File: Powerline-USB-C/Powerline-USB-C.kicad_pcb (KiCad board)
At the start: 2 copper layers, 14 x 100 mm, 17 parts, among them J1 USB-C 6pin, J2 Eurorack 10pin Power Connector, J3 Eurorack 10pin Power Connector, U1 CH224K, U2 N7812-1C, U3 N7812-1C

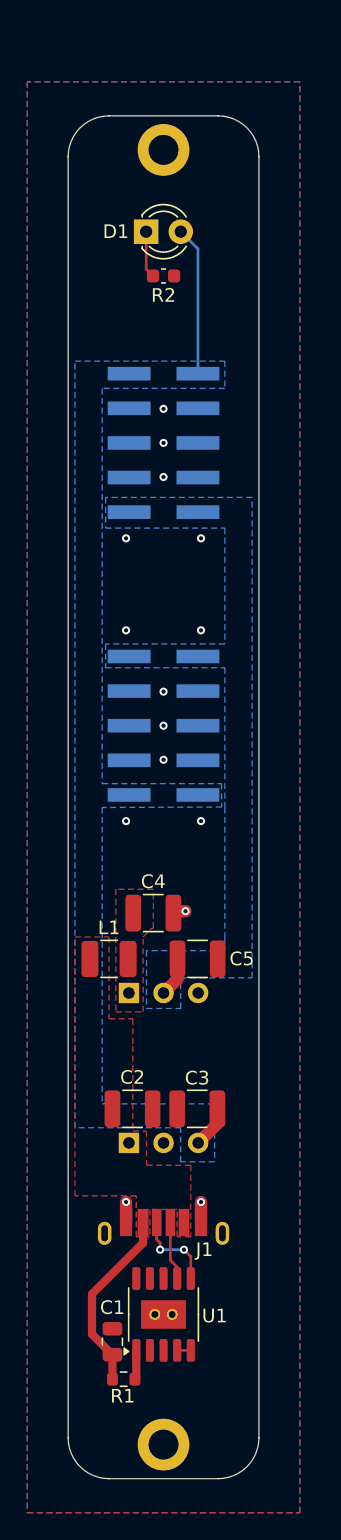
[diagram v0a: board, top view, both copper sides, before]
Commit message: minor hardware revision for main PCB
-changed two 10pin headers for singele 16pin header
-added 5V rail
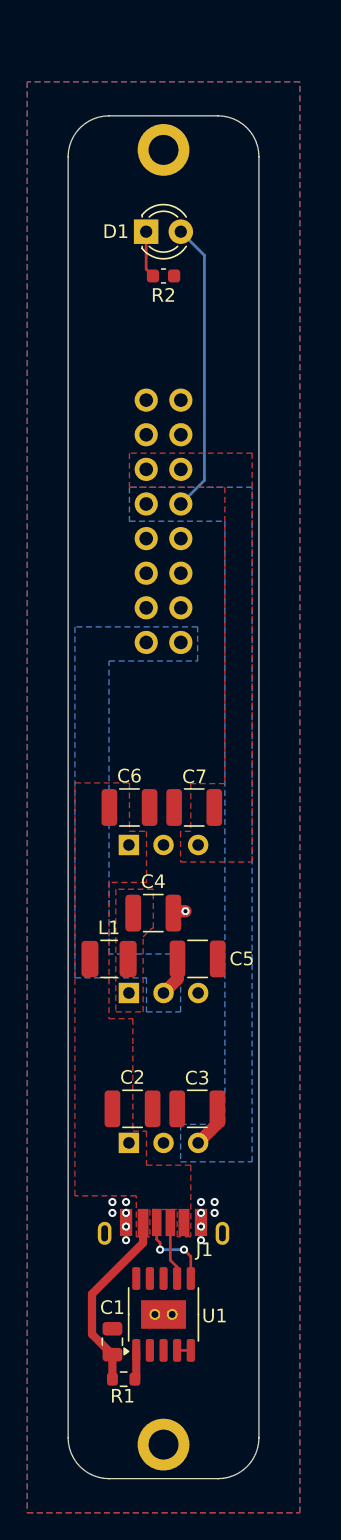
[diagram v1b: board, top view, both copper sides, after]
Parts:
- removed J3: Eurorack 10pin Power Connector, Powerline-USB-C:Eurorack shrouded 10 pin SMD header
- added C6: 10uF, Capacitor_SMD:C_1210_3225Metric, F.Cu at (76.5, 97.2)
- added C7: 22uF, Capacitor_SMD:C_1210_3225Metric, F.Cu at (81.2, 97.2)
- added U4: N7805-1C, Powerline-USB-C:N7812-1C, B.Cu at (79.0, 100.0)
- J2: value Eurorack 10pin Power Connector -> ~; footprint Powerline-USB-C:Eurorack shrouded 10 pin SMD header -> Powerline-USB-C:Keyed_16pin_Powerheader
- moved J2 15.0 mm to (79.0, 76.2)
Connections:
- J2 pad 2: -12V -> GND
- J2 pad 3: GND -> +12V
- J2 pad 4: GND -> +5V
- J2 pad 5: GND -> unconnected-(J2-CV-Pad5)
- J2 pad 6: GND -> unconnected-(J2-Gate-Pad6)_1
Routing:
- net +12V: track 14.1 -> 24.5 mm
- net GND: track 3.89 -> 0.89 mm, vias 15 -> 13
- added copper zone on F.Cu, net +5V

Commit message: Added 3D renders and fixed file structure
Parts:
- added REF**: Frontpanel, Powerline-USB-C:Frontpanel, F.Cu at (80.0, 88.8)
- moved C1 4.12 mm to (76.2, 132.4)
- moved C2 4.12 mm to (77.7, 115.4)
- moved C3 4.12 mm to (82.5, 115.4)
- moved C4 4.12 mm to (79.2, 101.0)
- moved C5 4.12 mm to (82.5, 104.4)
- moved C6 4.12 mm to (77.5, 93.2)
- moved C7 4.12 mm to (82.2, 93.2)
- moved D1 4.12 mm to (78.7, 51.0)
- moved H1 4.12 mm to (80.0, 45.0)
- moved H2 4.12 mm to (80.0, 140.0)
- moved J1 4.12 mm to (80.0, 124.5)
- moved J2 4.12 mm to (80.0, 72.2)
- moved L1 4.12 mm to (76.0, 104.4)
- moved R1 4.12 mm to (77.1, 135.2)
- moved R2 4.12 mm to (80.0, 54.2)
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
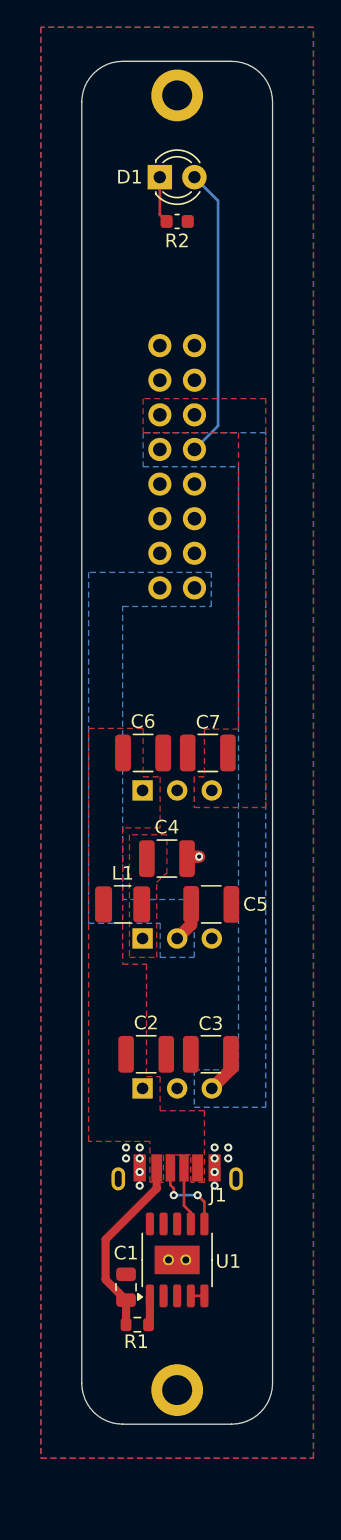
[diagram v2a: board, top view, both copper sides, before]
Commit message: update to kicad9
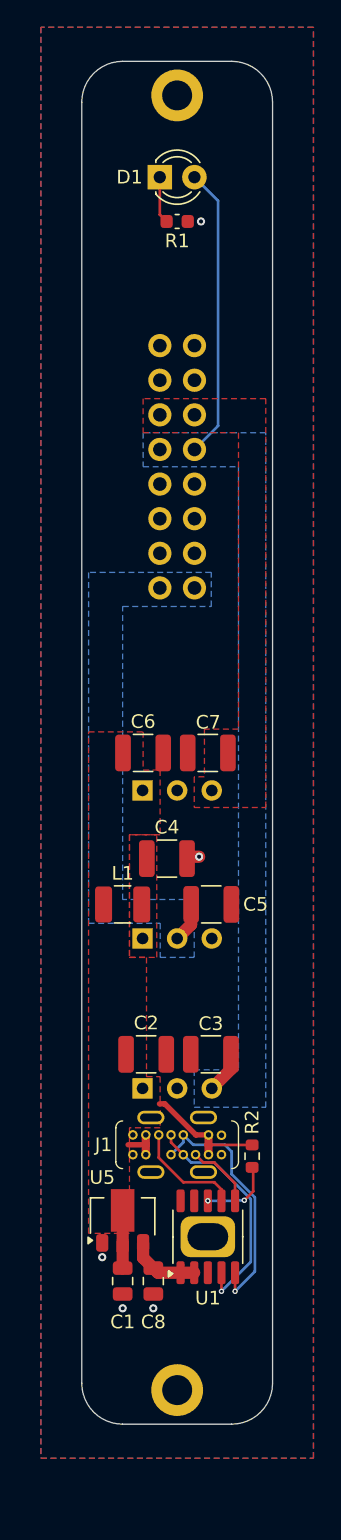
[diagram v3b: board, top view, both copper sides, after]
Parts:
- removed the R1 at (77.1, 135.2)
- added C8: 1uF, Capacitor_SMD:C_0805_2012Metric, F.Cu at (78.2, 132.0)
- added R2: 10K, Resistor_SMD:R_0603_1608Metric, F.Cu at (85.5, 122.8)
- added U5: HT7533-1, Powerline-USB-C:HT7533-1, F.Cu at (76.0, 127.2)
- H1, H2: value m2 mounting hole -> m2 mounting
- J1: value USB-C 6pin -> MC-802YC-H105; footprint Powerline-USB-C:6pin Vertical USB C connector -> Powerline-USB-C:USB-C
- U1: footprint Package_SO:SSOP-10-1EP_3.9x4.9mm_P1mm_EP2.1x3.3mm_ThermalVias -> Powerline-USB-C:CH224k
- moved U1 2.82 mm to (82.2, 128.8)
- moved J1 2.50 mm to (80.0, 122.0)
- moved REF** 0.79 mm to (80.2, 88.0)
- moved C1 0.51 mm to (76.0, 132.0), turned to -90 degrees
- renumbered R2 to R1
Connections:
- U1 pad 1: Net-(U1-VDD) -> +3.3V
- U1 pad 2: unconnected-(U1-CFG2-Pad2) -> +3.3V
- U1 pad 3: unconnected-(U1-CFG3-Pad3) -> GND
- U1 pad 4: Net-(U1-DM) -> Net-(U1-DP)
- U1 pad 8: unconnected-(U1-VBUS-Pad8) -> Net-(U1-VBUS)
- U1 pad 9: unconnected-(U1-CFG1-Pad9) -> GND
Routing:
- net Net-(U1-DM): track 1.00 -> 18.8 mm, vias 0 -> 1
- net Net-(U1-DP): track 0.00 -> 17.1 mm, vias 0 -> 1
- net Net-(U1-VBUS): track 0.00 -> 5.38 mm, vias 0 -> 2
- net +3.3V: track 0.00 -> 5.30 mm
- net Net-(J1-CC1): track 4.32 -> 8.08 mm
- net Net-(U1-VDD): track 2.01 -> 0.00 mm
- net Net-(J1-CC2): track 6.67 -> 5.05 mm, vias 2 -> 0
- net GND: vias 13 -> 5
